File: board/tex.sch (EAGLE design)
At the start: 267 parts, among them K1 HLS8L-DC5V-S-C, K2 HLS8L-DC5V-S-C, K3 HLS8L-DC5V-S-C, K4 HLS8L-DC5V-S-C, Q47 FDD4141, U14 24LC32A, U15 OPTO-LTV817, U16 OPTO-LTV817, U17 OPTO-LTV817, U18 OPTO-LTV817, U19 RELAY-S108T02PTH, U20 RELAY-S108T02PTH, U21 IO-HC4051, U5 AZ23C5V1, Y1 32.768KHz

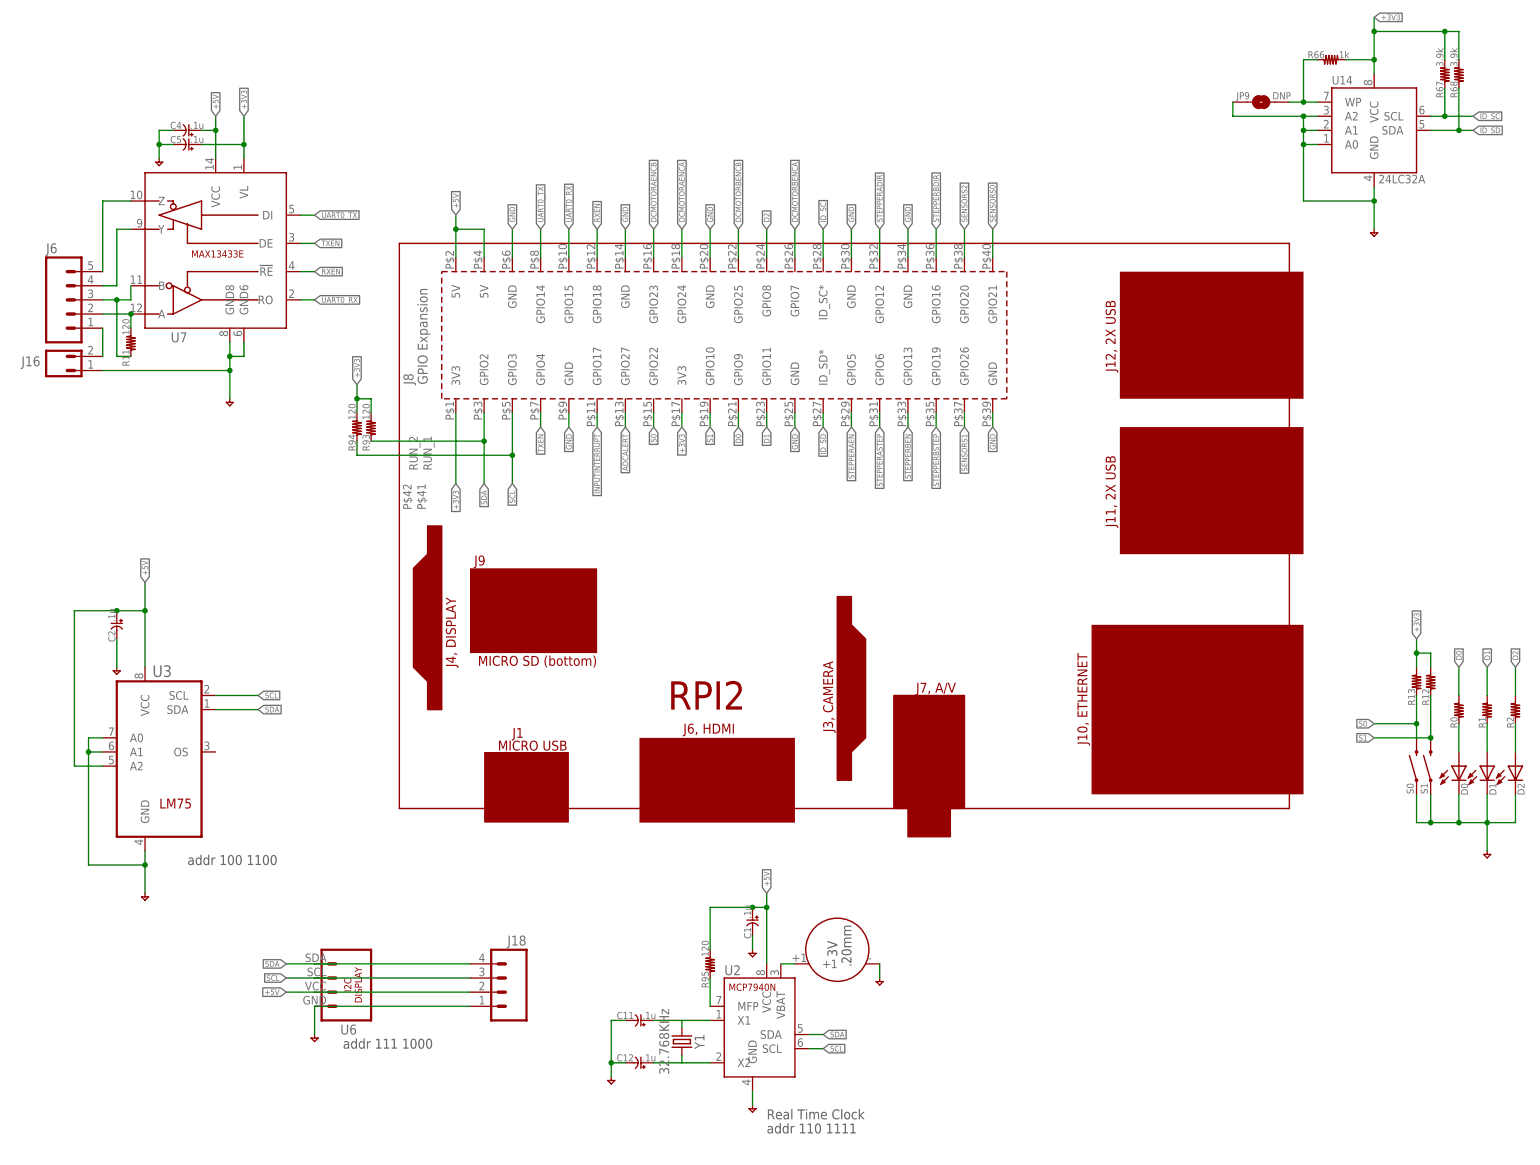
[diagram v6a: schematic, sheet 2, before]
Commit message: ready to place names
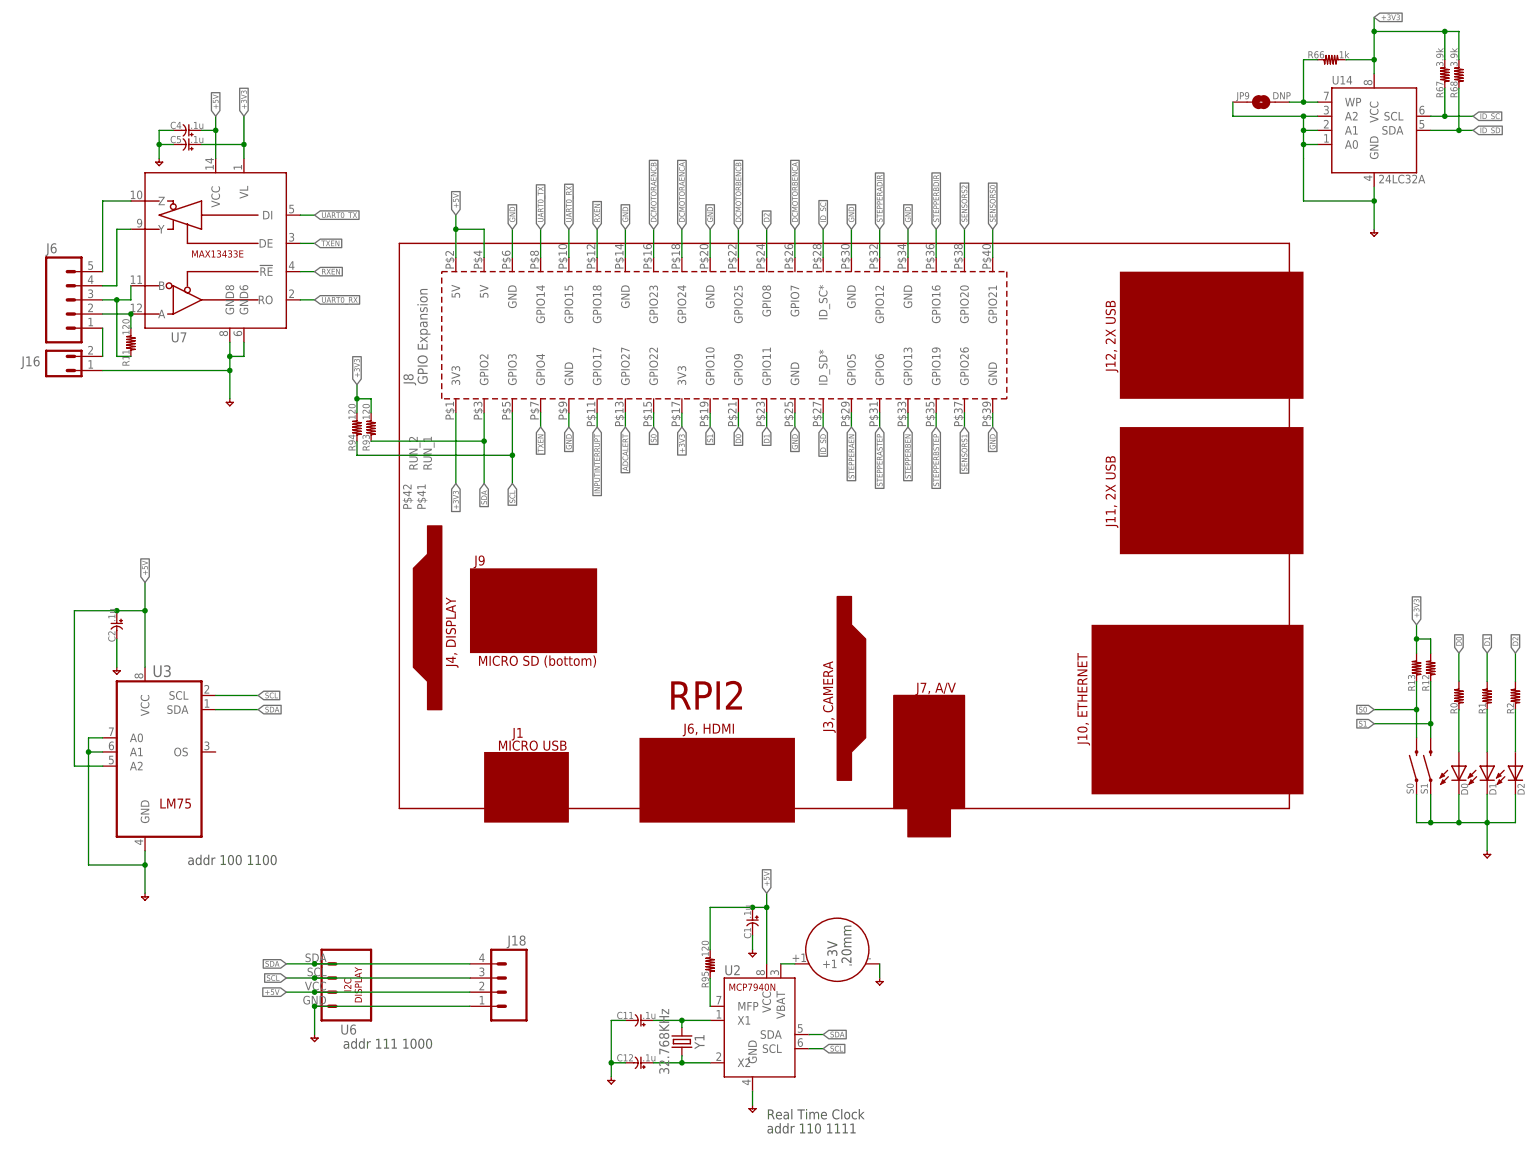
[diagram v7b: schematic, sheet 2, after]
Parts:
- added JP1, JP2: FIDUCIALUFIDUCIAL, holla:FIDUCIALUFIDUCIAL
- added TP1: (no value), holla:TESTPOINTTHRU
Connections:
- removed net ADC0_3: U8.AIN3
- net AGND: now also U8.AIN3
- net GND: now also TP1.P$1, U2.GND
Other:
- note added: "ENCODER"
- note added: "I2C Address Table 010 0000 I/O MCP23107 100 0000 VBATT Current Sense INA219 100 1000 ADC ADS1015 100 1100 TEMP LM75 110 0000 LED PCA9685 110 1111 RTC MCP7940 111 1000 Display SSD1306 Banggood"
- note added: "Relays can be VBATT voltage or +5V, install 0ohm resistor to select"
- note added: "ToDo List"
- note removed: "AGND not implemented, not high-performance design I2C Address Table 010 0000 I/O MCP23107 100 0000 VBATT Current Sense INA219 100 1000 ADC ADS1015 100 1100 TEMP LM75 110 0000 LED PCA9685 110 1111 RTC MCP7940 111 1000 Display SSD1306 Banggood"
- note removed: "SPI"
- note removed: "connect adc alert to rpi does ina219 give the vbatt voltage? do something adc0_3"
- note removed: "put down analog gnds add +5V out connector for stepper driver"
- moved on the sheet: C30, C34, C35, C36, C37, R0, R1, R12, R13, R2, R6, R7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

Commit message: board file submission
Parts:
- removed C35, C38: (no value), holla:C-USC0603
- removed D0, D37: (no value), holla:LED-0603
- removed J31: (no value), holla:M06-PLUGIN-SCREW
- removed J32: (no value), holla:M05-PLUGIN-SCREW
- removed JP9: DNP, holla:JUMPER-PAD-2-NO
- removed R0: (no value), holla:R-US_R0603
- removed R95: 120, holla:R-US_R0603
- removed S0: (no value), holla:SWITCH-PUSHBUTTON-6MMX3.5MM
- removed U21: IO-HC4051, holla:IO-HC4051
- removed U22: (no value), holla:IO-MCP23017SO
- added C13, C14: .1u, holla:C-USC0603
- added D3, D7: (no value), holla:LED-0603
- added J20: (no value), holla:M02-6.35MM
- added J22: (no value), holla:M02-PLUGIN-SCREW
- added JP3: FIDUCIALUFIDUCIAL, holla:FIDUCIALUFIDUCIAL
- added R14, R15: (no value), holla:R-US_R0603
- added S2: (no value), holla:SWITCH-PUSHBUTTON-6MMX3.5MM
- added U12: OPTO-LTV817, holla:OPTO-LTV817
- added U9: (no value), holla:DCDC-CONVERTER-LM2577-BOARD
- C10, C3: value (none) -> .1u
- C11, C15, C17, C2: value .1u -> (none)
- D21, D22, D23, D24: device holla:LED-0603 -> holla:DIODE-0603
- D28, D29, D30: device holla:DIODE-0603 -> holla:LED-0603
- D31: device holla:DIODE-0603 -> holla:DIODE-SMA
- D35, D36: device holla:LED-0603 -> holla:DIODE-0805
- D4: device holla:DIODE-SMA -> holla:LED-0603
- D5, D6: device holla:DIODE-0805 -> holla:LED-0603
- J1: device holla:M02-6.35MM -> holla:M04-PLUGIN-SCREW
- J10, J27, J28: device holla:M02-PLUGIN-SCREW -> holla:M03-PLUGIN-SCREW
- J11: device holla:M03-PLUGIN-SCREW -> holla:M04-0.1
- J12: device holla:M03-PLUGIN-SCREW -> holla:M02-0.1
- J13: device holla:M03-PLUGIN-SCREW -> holla:M05-PLUGIN-SCREW
- J14: device holla:M03-PLUGIN-SCREW -> holla:M04-PLUGIN-SCREW
- J15: device holla:M02-PLUGIN-SCREW -> holla:M04-PLUGIN-SCREW
- J16: device holla:M02-0.1 -> holla:M06-PLUGIN-SCREW
- J17: device holla:M06-PLUGIN-SCREW -> holla:M05-PLUGIN-SCREW
- J18: device holla:M04-0.1 -> holla:M05-PLUGIN-SCREW
- J21: device holla:M06-PLUGIN-SCREW -> holla:M02-PLUGIN-SCREW
- J29, J30: device holla:M03-PLUGIN-SCREW -> holla:M06-PLUGIN-SCREW
- J5: device holla:M04-PLUGIN-SCREW -> holla:M02-PLUGIN-SCREW
- J6: device holla:M05-PLUGIN-SCREW -> holla:M02-PLUGIN-SCREW
- J7: device holla:M05-PLUGIN-SCREW -> holla:M03-PLUGIN-SCREW
- J8, J9: device holla:M04-PLUGIN-SCREW -> holla:M03-PLUGIN-SCREW
- JP2: value FIDUCIALUFIDUCIAL -> DNP; device holla:FIDUCIALUFIDUCIAL -> holla:JUMPER-PAD-2-NO
- Q1, Q3: device holla:FET-NCHANNEL-SOT23 -> holla:FET-NCHANNEL-TO252
- Q12, Q14, Q16, Q18, Q20, Q33, Q36: device holla:FET-PCHANNEL-TO252 -> holla:FET-NCHANNEL-SOT23
- Q2, Q4: device holla:FET-PCHANNEL-TO252 -> holla:FET-NCHANNEL-TO252
- Q21, Q23, Q25, Q28, Q5, Q7, Q9: device holla:FET-NCHANNEL-SOT23 -> holla:FET-PCHANNEL-TO252
- Q26, Q29: device holla:FET-NCHANNEL-TO252 -> holla:FET-PCHANNEL-TO252
- Q32, Q35: device holla:FET-NCHANNEL-TO252 -> holla:FET-NCHANNEL-SOT23
- Q41: value (none) -> FDD4141; device holla:FET-NCHANNEL-SOT23 -> brightleaf:FDD4141TO252
- Q47: value FDD4141 -> (none); device brightleaf:FDD4141TO252 -> holla:FET-NCHANNEL-SOT23
- R10: value 47k -> (none)
- R11, R93, R94: value 120 -> (none)
- R19: value (none) -> 0
- R20, R21, R29, R31, R32, R66: value 1k -> (none)
- R22, R91: value 0 -> (none)
- R23, R90: value DNP -> (none)
- R24, R30: value 10k -> (none)
- R28: value 1k -> DNP
- R33: value 10k -> (none); device holla:R-US_R0603 -> holla:R-US_R1210
- R34, R51: device holla:R-US_R0603 -> holla:R-US_R1210
- R39, R40, R52: value (none) -> 120
- R43: value (none) -> 47k
- R44, R55, R56, R57, R71, R72, R77: value (none) -> 1k
- R53, R54, R69: value (none) -> 10k
- R59: device holla:R-US_R1210 -> holla:R-US_R0603
- R63: value (none) -> 0; device holla:R-US_R1210 -> holla:R-US_R0603
- R67, R68: value 3.9k -> (none)
- R70: value (none) -> DNP
- R73, R74: value (none) -> 3.9k
- R79: value (none) -> 120; device holla:R-US_R1210 -> holla:R-US_R0603
- U1: value (none) -> RELAY-S108T02PTH; device holla:DCDC-CONVERTER-LM2577-BOARD -> holla:RELAY-S108T02PTH
- U10: device holla:AMP-OPAMP-DUAL-SO08 -> holla:ADC-ADS1015-MSOP10
- U13: value (none) -> OPTO-LTV817; device holla:IO-PCA9685-TSSOP28 -> holla:OPTO-LTV817
- U14: value 24LC32A -> OPTO-LTV817; device holla:MEMORY-EEPROM-SO08 -> holla:OPTO-LTV817
- U16: value OPTO-LTV817 -> (none); device holla:OPTO-LTV817 -> holla:IO-MCP23017SO
- U17: value OPTO-LTV817 -> 24LC32A; device holla:OPTO-LTV817 -> holla:MEMORY-EEPROM-SO08
- U18: value OPTO-LTV817 -> IO-HC4051; device holla:OPTO-LTV817 -> holla:IO-HC4051
- U19: value RELAY-S108T02PTH -> (none); device holla:RELAY-S108T02PTH -> holla:RTC-MCP7940N
- U2: value (none) -> RELAY-S108T02PTH; device holla:RTC-MCP7940N -> holla:RELAY-S108T02PTH
- U20: value RELAY-S108T02PTH -> (none); device holla:RELAY-S108T02PTH -> holla:DISP-I2C-4PIN
- U3: device holla:SENSOR-TEMP-LM75-SO08 -> holla:COMM-MAX13433E
- U4: value (none) -> AZ23C5V1; device holla:ADC-INA219-SOIC8 -> brightleaf:AZ23CXXX
- U5: value AZ23C5V1 -> (none); device brightleaf:AZ23CXXX -> holla:IO-PCA9685-TSSOP28
- U6: device holla:DISP-I2C-4PIN -> holla:AMP-OPAMP-DUAL-SO08
- U7: device holla:COMM-MAX13433E -> holla:ADC-INA219-SOIC8
- U8: device holla:ADC-ADS1015-MSOP10 -> holla:SENSOR-TEMP-LM75-SO08
- renumbered B1 to B100, C30 to C19, C31 to C18, C34 to C23, C36 to C21, C37 to C20
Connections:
- net +3V3: now also C1.1, R39.2, R40.2, R41.2, R42.2, R73.2, R74.2, R77.2, U17.VCC, U3.VL; no longer C5.1, R12.2, R13.2, R66.2, R67.2, R68.2, R93.2, R94.2, U14.VCC, U7.VL
- net +5V: now also C16.1, C6.1, C8.1, J11.2, J16.4, J16.5, J16.6, J17.5, J18.5, J27.3, J28.3, J30.6, R28.2, R78.1, R79.2, U1.+, U16.!RESET, U16.VDD, U19.VCC, U2.+, U20.VCC, U5.A5, U5.VCC, U7.VS, U8.A2, U8.VCC, U9.VOUT+; no longer C1.1, C22.1, C4.1, J18.2, J19.4, J19.5, J19.6, J29.3, J30.3, J31.6, J32.5, J7.5, R3.1, R90.2, R95.2, U1.VOUT+, U13.A5, U13.VCC, U19.+, U2.VCC, U20.+, U22.!RESET, U22.VDD, U3.A2, U4.VS, U6.VCC, U7.VCC
- net ADC0_1: now also R53.2, U10.AIN1, U6A.OUT; no longer R30.2, U10A.OUT, U8.AIN1
- net ADC0_2: now also R54.2, U10.AIN2, U6B.OUT; no longer R33.2, U10B.OUT, U8.AIN2
- net ADCALERT: now also U10.ALERT; no longer U8.ALERT
- net AGND: now also C11.2, C12.2, C22.2, C4.2, C5.2, J21.1, J22.1, R55.1, R56.1, R59.1, R64.2, R70.1, R71.1, R75.1, R87.1, R89.1, U10.ADDR, U10.AIN3, U10.GND, U18.!E, U18.GND, U18.VEE, U6A.V-; no longer C16.2, C35.2, C38.2, C6.2, C8.2, J29.1, J30.1, R17.1, R19.1, R21.1, R23.1, R25.2, R27.1, R28.1, R31.1, R5.1, U10A.V-, U21.!E, U21.GND, U21.VEE, U8.ADDR, U8.AIN3, U8.GND
- net AVCC: now also C15.1, C5.1, C7.1, R78.2, R90.2, R91.2, R93.2, R94.2, U10.VCC, U18.VCC, U6A.V+; no longer C16.1, C38.1, C8.1, R3.2, R6.2, R7.2, R8.2, R9.2, U10A.V+, U21.VCC, U8.VCC
- net D0: now also R60.2; no longer R0.2
- net D1: now also R61.2; no longer R1.2
- net D2: now also R62.2; no longer R2.2
- net DCMOTORAENCA: now also U14.4; no longer U15.4
- net DCMOTORAENCB: now also U15.4; no longer U16.4
- net DCMOTORBENCA: now also U12.4; no longer U17.4
- net DCMOTORBENCB: now also U13.4; no longer U18.4
- net GND: now also C13.2, C14.2, C16.2, C6.2, C8.2, D31.A, D32.C, D33.C, D34.C, J11.1, J12.1, J14.4, J15.4, J17.1, J19.1, J19.2, J19.3, J19.4, J19.5, J19.6, J20.1, J30.1, JP2.1, Q12.S, Q14.S, Q16.S, Q18.S, Q20.S, Q32.S, Q33.S, Q35.S, Q36.S, Q47.S, R1.1, R10.1, R11.1, R12.1, R13.1, R14.1, R16.1, R17.1, R2.1, R3.1, R33.2, R34.2, R4.1, R43.2, R5.1, R6.1, R64.1, R7.1, R8.1, R80.1, R81.1, R82.1, R83.1, R84.1, R85.1, R9.1, S2.1, U12.2, U12.3, U13.2, U13.3, U14.2, U14.3, U16.A0, U16.A1, U16.A2, U16.VSS, U17.A0, U17.A1, U17.A2, U17.GND, U19.GND, U20.GND, U3.GND6, U3.GND8, U5.!OE, U5.A0, U5.A1, U5.A2, U5.A3, U5.A4, U5.EXTCLK, U5.GND, U7.A0, U7.A1, U7.GND, U8.A0, U8.A1, U8.GND, U9.VIN-, U9.VOUT-; no longer C11.2, C12.2, C22.2, C4.2, C5.2, D0.C, D1.C, D2.C, D4.A, J1.1, J16.1, J21.1, J21.2, J21.3, J21.4, J21.5, J21.6, J31.1, J32.1, J7.1, J8.4, J9.4, JP9.1, Q1.S, Q21.S, Q23.S, Q25.S, Q28.S, Q3.S, Q41.S, Q5.S, Q7.S, Q9.S, R10.2, R25.1, R35.1, R37.1, R39.1, R41.1, R43.1, R45.1, R47.1, R49.1, R51.1, R53.1, R55.1, R57.1, R59.2, R63.2, R69.1, R70.1, R71.1, R72.1, R73.1, R74.1, R75.1, R76.1, R77.1, R78.1, S0.1, U1.VIN-, U1.VOUT-, U13.!OE, U13.A0, U13.A1, U13.A2, U13.A3, U13.A4, U13.EXTCLK, U13.GND, U14.A0, U14.A1, U14.A2, U14.GND, U16.2, U16.3, U17.2, U17.3, U18.2, U18.3, U2.GND, U22.A0, U22.A1, U22.A2, U22.VSS, U3.A0, U3.A1, U3.GND, U4.A0, U4.A1, U4.GND, U6.GND, U7.GND6, U7.GND8
- net GND4: now also D21.A, D27.C, K2.V-, Q18.D; no longer D31.A, D35.C, K4.V-, Q46.D
- net ID_SC: now also R73.1, U17.SCL; no longer R67.1, U14.SCL
- net ID_SD: now also R74.1, U17.SDA; no longer R68.1, U14.SDA
- net INPUTINTERRUPT: now also U16.INTB; no longer U22.INTB
- net MOTORA_SENSE: now also Q1.S, Q2.S, R33.1, R44.1; no longer Q32.S, Q35.S, R29.1, R63.1
- net MOTORB_SENSE: now also Q3.S, Q4.S, R34.1, R57.1; no longer Q26.S, Q29.S, R32.1, R59.1
- net N$1: now also Q40.G, U5.PWM0; no longer Q1.G, U13.PWM0
- net N$100: now also D6.C, R3.2; no longer D18.C, R55.2
- net N$101: now also J20.2; no longer J1.2
- net N$102: now also C29.1, J29.1, U16.GPB2; no longer C24.1, J17.1, U22.GPB2
- net N$103: now also C28.1, J29.2, U16.GPB3; no longer C25.1, J17.2, U22.GPB3
- net N$104: now also JP2.2, R77.1, U17.WP; no longer JP9.2, R66.1, U14.WP
- net N$105: now also R53.1, R56.2, U6A.-IN; no longer R28.2, R30.1, U10A.-IN
- net N$107: now also C9.1, R57.2, U6B.+IN; no longer C17.1, R32.2, U10B.+IN
- net N$108: now also C27.1, J29.3, U16.GPB4; no longer C26.1, J17.3, U22.GPB4
- net N$109: now also C26.1, J29.4, U16.GPB5; no longer C27.1, J17.4, U22.GPB5
- net N$111: now also C25.1, J29.5, U16.GPB6; no longer C28.1, J17.5, U22.GPB6
- net N$114: now also C24.1, J29.6, U16.GPB7; no longer C29.1, J17.6, U22.GPB7
- net N$118: now also U19.VBAT; no longer U2.VBAT
- net N$120: now also J28.2, R90.1, U18.Y0; no longer J30.2, R92.1, U21.Y0
- net N$124: now also R88.1, R89.2, U18.Y1; no longer R18.1, R19.2, U21.Y1
- net N$13: now also J13.2, R52.2, U3.A; no longer J6.2, R11.2, U7.A
- net N$130: now also C17.1, R86.1, R87.2, U18.Y2; no longer C6.1, R4.1, R5.2, U21.Y2
- net N$138: now also C11.1, R75.2, R76.1; no longer C7.1, R16.1, R17.2
- net N$139: now also D7.C, R4.2; no longer D17.C, R53.2
- net N$14: now also J13.3, R52.1, U3.B; no longer J6.3, R11.1, U7.B
- net N$140: now also D8.C, R5.2; no longer D16.C, R51.2
- net N$141: now also D9.C, R6.2; no longer D15.C, R49.2
- net N$142: now also D10.C, R7.2; no longer D14.C, R47.2
- net N$143: now also J10.2, K4.COM; no longer J14.2, K1.COM
- net N$144: now also J10.1, K4.NO; no longer J14.1, K1.NO
- net N$145: now also J10.3, K4.NC; no longer J14.3, K1.NC
- net N$146: now also D11.C, R8.2; no longer D13.C, R45.2
- net N$147: now also D29.A, R31.1; no longer D33.A, R85.1
- net N$148: now also R67.1, U14.1; no longer R80.1, U15.1
- net N$149: now also J15.3, R68.2; no longer J8.3, R81.2
- net N$15: now also J13.4, U3.Y; no longer J6.4, U7.Y
- net N$150: now also J15.2, R67.2; no longer J8.2, R80.2
- net N$151: now also J17.2, Q42.D; no longer J32.2, Q39.D
- net N$152: now also J18.4, Q47.D; no longer J7.4, Q40.D
- net N$153: now also J18.3, Q46.D; no longer J7.3, Q41.D
- net N$154: now also J18.2, Q45.D; no longer J7.2, Q42.D
- net N$155: now also R68.1, U15.1; no longer R81.1, U16.1
- net N$156: now also J14.2, R65.2; no longer J9.2, R82.2
- net N$157: now also J14.3, R66.2; no longer J9.3, R83.2
- net N$158: now also R65.1, U12.1; no longer R82.1, U17.1
- net N$159: now also D22.A, D28.C, K1.V-, Q19.D; no longer D30.A, D34.C, K3.V-, Q45.D
- net N$16: now also J13.5, U3.Z; no longer J6.5, U7.Z
- net N$161: now also D23.A, D29.C, K3.V-, Q17.D; no longer D29.A, D33.C, K2.V-, Q44.D
- net N$162: now also R66.1, U13.1; no longer R83.1, U18.1
- net N$163: now also J9.2, K3.COM; no longer J11.2, K2.COM
- net N$164: now also J9.1, K3.NO; no longer J11.1, K2.NO
- net N$165: now also J9.3, K3.NC; no longer J11.3, K2.NC
- net N$166: now also J8.2, K1.COM; no longer J12.2, K3.COM
- net N$167: now also J8.1, K1.NO; no longer J12.1, K3.NO
- net N$168: now also J8.3, K1.NC; no longer J12.3, K3.NC
- net N$169: now also J7.1, K2.NO; no longer J13.1, K4.NO
- net N$17: now also J12.2, J13.1; no longer J16.2, J6.1
- net N$170: now also J7.2, K2.COM; no longer J13.2, K4.COM
- net N$171: now also J7.3, K2.NC; no longer J13.3, K4.NC
- net N$172: now also D21.C, D22.C, D23.C, D24.C, R19.1, R28.1, R29.2, R30.2, R31.2, R32.2; no longer D28.C, D29.C, D30.C, D31.C, R84.2, R85.2, R86.2, R87.2, R90.1, R91.1
- net N$173: now also D30.A, R32.1; no longer D32.A, R84.1
- net N$174: now also D28.A, R30.1; no longer D34.A, R86.1
- net N$175: now also D27.A, R29.1; no longer D35.A, R87.1
- net N$176: now also D24.A, D30.C, K4.V-, Q20.D; no longer D28.A, D32.C, K1.V-, Q43.D
- net N$177: now also J6.2, U2.T2; no longer J10.2, U19.T2
- net N$178: now also J5.1, U1.T1; no longer J15.1, U20.T1
- net N$179: now also J5.2, U1.T2; no longer J15.2, U20.T2
- net N$180: now also D26.C, R26.2; no longer D36.C, R88.2
- net N$181: now also D25.C, R25.2; no longer D37.C, R89.2
- net N$182: now also D26.A, U2.-; no longer D36.A, U19.-
- net N$183: now also D25.A, U1.-; no longer D37.A, U20.-
- net N$184: now also J24.2, R94.1, U18.Y4; no longer J26.2, R6.1, U21.Y4
- net N$185: now also C22.1, J23.2, R93.1, U18.Y5; no longer C35.1, J25.2, R7.1, U21.Y5
- net N$186: now also J22.2, R92.1, U18.Y6; no longer J24.2, R8.1, U21.Y6
- net N$187: now also J21.2, R91.1, U18.Y7; no longer J23.2, R9.1, U21.Y7
- net N$188: now also R58.2, R63.2; no longer R22.2, R26.2
- net N$189: now also R72.1, U18.Z; no longer R20.1, U21.Z
- net N$190: now also R58.1, R59.2, U10.AIN0; no longer R26.1, R27.2, U8.AIN0
- net N$191: now also R69.2, U18.Y3; no longer R24.2, U21.Y3
- net N$192: now also R79.1, U19.MFP; no longer R95.1, U2.MFP
- net N$194: now also Q41.D; no longer Q47.D
- net N$2: now also D35.C, R86.2; no longer D5.C, R4.2
- net N$20: now also D35.A, J26.2; no longer D5.A, J28.2
- net N$25: now also D36.C, R76.2; no longer D6.C, R16.2
- net N$26: now also D36.A, J25.2; no longer D6.A, J27.2
- net N$27: now also J27.2, R88.2; no longer J29.2, R18.2
- net N$29: now also D32.A, R60.1; no longer D0.A, R0.1
- net N$3: now also C13.1, U19.X1; no longer C11.1, U2.X1
- net N$30: now also D33.A, R61.1; no longer D1.A, R1.1
- net N$31: now also D34.A, R62.1; no longer D2.A, R2.1
- net N$35: now also Q12.D, Q6.G, R20.1; no longer Q19.D, Q20.G, R52.1
- net N$36: now also Q26.G, Q36.D, R45.1; no longer Q17.D, Q18.G, R50.1
- net N$37: now also Q13.D, Q7.G, R21.1; no longer Q15.D, Q16.G, R48.1
- net N$38: now also R63.1, R70.2; no longer R22.1, R23.2
- net N$39: now also R69.1, R71.2; no longer R21.2, R24.1
- net N$4: now also Q41.G, R43.1, U4.A; no longer Q47.G, R10.1, U5.A
- net N$40: now also Q27.G, Q37.D, R47.1; no longer Q13.D, Q14.G, R46.1
- net N$41: now also Q14.D, Q8.G, R22.1; no longer Q11.D, Q12.G, R44.1
- net N$42: now also Q28.G, Q38.D, R48.1; no longer Q10.G, Q9.D, R42.1
- net N$43: now also Q15.D, Q9.G, R23.1; no longer Q7.D, Q8.G, R40.1
- net N$44: now also Q29.G, Q39.D, R49.1; no longer Q5.D, Q6.G, R38.1
- net N$45: now also Q10.G, Q16.D, R24.1; no longer Q3.D, Q4.G, R36.1
- net N$46: now also Q30.G, Q40.D, R50.1; no longer Q1.D, Q2.G, R34.1
- net N$47: now also Q16.G, U5.PWM1; no longer Q3.G, U13.PWM1
- net N$48: now also Q39.G, U5.PWM2; no longer Q5.G, U13.PWM2
- net N$49: now also Q15.G, U5.PWM3; no longer Q7.G, U13.PWM3
- net N$5: now also C14.1, U19.X2; no longer C12.1, U2.X2
- net N$50: now also Q38.G, U5.PWM4; no longer Q9.G, U13.PWM4
- net N$51: now also Q14.G, U5.PWM5; no longer Q11.G, U13.PWM5
- net N$52: now also Q37.G, U5.PWM6; no longer Q13.G, U13.PWM6
- net N$53: now also Q13.G, U5.PWM7; no longer Q15.G, U13.PWM7
- net N$54: now also Q36.G, U5.PWM8; no longer Q17.G, U13.PWM8
- net N$55: now also C12.1, R72.2; no longer C9.1, R20.2
- net N$56: now also Q12.G, U5.PWM9; no longer Q19.G, U13.PWM9
- net N$57: now also D2.A, J1.2, Q2.D, Q22.D, R15.2; no longer D26.A, J5.2, Q32.D, Q33.D, R64.2
- net N$58: now also Q2.G, Q22.G, Q33.D, R37.1; no longer Q31.D, Q32.G, Q33.G, R62.1
- net N$59: now also D1.A, D17.C, D19.A, J1.1, Q1.D, Q21.D; no longer D22.C, D23.A, D27.A, J5.1, Q35.D, Q36.D
- net N$6: now also J30.2, U16.GPA6; no longer J31.2, U22.GPA6
- net N$60: now also Q1.G, Q21.G, Q32.D, R36.1; no longer Q34.D, Q35.G, Q36.G, R65.1
- net N$61: now also Q32.G, U5.PWM15; no longer Q34.G, U13.PWM15
- net N$62: now also Q33.G, U5.PWM14; no longer Q31.G, U13.PWM14
- net N$63: now also D4.A, J1.4, Q24.D, Q4.D, R18.2; no longer D25.A, J5.4, Q26.D, Q27.D, R60.2
- net N$64: now also Q24.G, Q31.D, Q4.G, R35.1; no longer Q25.D, Q26.G, Q27.G, R58.1
- net N$65: now also D16.A, J4.4, Q30.D; no longer D8.A, J2.4, Q2.D
- net N$66: now also D15.A, J4.3, Q10.D; no longer D9.A, J2.3, Q4.D
- net N$67: now also D14.A, J4.2, Q29.D; no longer D10.A, J2.2, Q6.D
- net N$68: now also D13.A, J4.1, Q9.D; no longer D11.A, J2.1, Q8.D
- net N$69: now also Q28.D; no longer Q10.D
- net N$7: now also J30.5, U16.GPB1; no longer J31.5, U22.GPB1
- net N$70: now also D11.A, Q8.D; no longer D13.A, Q12.D
- net N$71: now also D10.A, Q27.D; no longer D14.A, Q14.D
- net N$72: now also D9.A, Q7.D; no longer D15.A, Q16.D
- net N$73: now also D8.A, J2.4, Q26.D; no longer D16.A, J4.4, Q18.D
- net N$74: now also D7.A, J2.3, Q6.D; no longer D17.A, J4.3, Q20.D
- net N$75: now also D13.C, R10.2; no longer D11.C, R41.2
- net N$76: now also J6.1, U2.T1; no longer J10.1, U19.T1
- net N$77: now also R9.2; no longer R43.2
- net N$78: now also D1.C, R14.2; no longer D27.C, R72.2
- net N$79: now also D2.C, R16.2; no longer D26.C, R71.2
- net N$8: now also J30.4, U16.GPB0; no longer J31.4, U22.GPB0
- net N$80: now also D3.C, R17.2; no longer D24.C, R69.2
- net N$81: now also D4.C, R1.2; no longer D25.C, R70.2
- net N$82: now also D14.C, R11.2; no longer D10.C, R39.2
- net N$83: now also D15.C, R12.2; no longer D9.C, R37.2
- net N$84: now also D16.C, R13.2; no longer D8.C, R35.2
- net N$85: now also D18.C, D20.A, D3.A, J1.3, Q23.D, Q3.D; no longer D20.C, D21.A, D24.A, J5.3, Q29.D, Q30.D
- net N$86: now also Q23.G, Q3.G, Q34.D, R38.1; no longer Q28.D, Q29.G, Q30.G, R61.1
- net N$87: now also Q34.G, U5.PWM13; no longer Q28.G, U13.PWM13
- net N$88: now also Q31.G, U5.PWM12; no longer Q25.G, U13.PWM12
- net N$89: now also D18.A, D20.C, R18.1; no longer D20.A, D21.C, R60.1
- net N$9: now also J30.3, U16.GPA7; no longer J31.3, U22.GPA7
- net N$90: now also Q35.G, U5.PWM10; no longer Q21.G, U13.PWM10
- net N$91: now also Q11.G, U5.PWM11; no longer Q23.G, U13.PWM11
- net N$92: now also D17.A, D19.C, R15.1; no longer D22.A, D23.C, R64.1
- net N$93: now also D6.A, J2.2, Q25.D; no longer D18.A, J4.2, Q22.D
- net N$94: now also D5.A, J2.1, Q5.D; no longer D19.A, J4.1, Q24.D
- net N$95: now also Q11.D, Q5.G, R27.1; no longer Q23.D, Q24.G, R56.1
- net N$96: now also Q25.G, Q35.D, R46.1; no longer Q21.D, Q22.G, R54.1
- net N$97: now also C4.1, R44.2, U6A.+IN; no longer C15.1, R29.2, U10A.+IN
- net N$98: now also D5.C, R2.2; no longer D19.C, R57.2
- net N$99: now also R54.1, R55.2, U6B.-IN; no longer R31.2, R33.1, U10B.-IN
- net RELAY0EN: now also Q20.G, U16.GPA0; no longer Q43.G, U22.GPA0
- net RELAY1EN: now also Q17.G, U16.GPA1; no longer Q44.G, U22.GPA1
- net RELAY2EN: now also Q19.G, U16.GPA2; no longer Q45.G, U22.GPA2
- net RELAY3EN: now also Q18.G, U16.GPA3; no longer Q46.G, U22.GPA3
- net RELAY4EN: now also R26.1, U16.GPA4; no longer R88.1, U22.GPA4
- net RELAY5EN: now also R25.1, U16.GPA5; no longer R89.1, U22.GPA5
- net RXEN: now also U3.!RE; no longer U7.!RE
- net S0: now also R41.1, S1.2; no longer R13.1, S0.2
- net S1: now also R42.1, S2.2; no longer R12.1, S1.2
- net SCL: now also J11.3, R40.1, U10.SCL, U16.SCL, U19.SCL, U20.SCL, U5.SCL, U7.SCL; no longer J18.3, R94.1, U13.SCL, U2.SCL, U22.SCL, U3.SCL, U4.SCL, U6.SCL
- net SDA: now also J11.4, R39.1, U10.SDA, U16.SDA, U19.SDA, U20.SDA, U5.SDA, U7.SDA; no longer J18.4, R93.1, U13.SDA, U2.SDA, U22.SDA, U3.SDA, U4.SDA, U6.SDA
- net SENSORS0: now also U18.S0; no longer U21.S0
- net SENSORS1: now also U18.S1; no longer U21.S1
- net SENSORS2: now also U18.S2; no longer U21.S2
- net STEPPER1DIROUT: now also J17.3, Q43.D; no longer J32.3, Q38.D
- net STEPPER1ENOUT: now also J17.4, Q44.D; no longer J32.4, Q37.D
- net STEPPERADIR: now also Q46.G, R84.2; no longer Q41.G, R77.2
- net STEPPERAEN: now also Q47.G, R85.2; no longer Q40.G, R76.2
- net STEPPERASTEP: now also Q45.G, R83.2; no longer Q42.G, R78.2
- net STEPPERBDIR: now also Q43.G, R81.2; no longer Q38.G, R74.2
- net STEPPERBEN: now also Q44.G, R82.2; no longer Q37.G, R73.2
- net STEPPERBSTEP: now also Q42.G, R80.2; no longer Q39.G, R75.2
- net TXEN: now also U3.DE; no longer U7.DE
- net UART0_RX: now also U3.RO; no longer U7.RO
- net UART0_TX: now also U3.DI; no longer U7.DI
- net VBATT: now also D31.C, J14.1, J15.1, J16.1, J16.2, J16.3, Q21.S, Q23.S, Q25.S, Q26.S, Q28.S, Q29.S, Q5.S, Q7.S, Q9.S, R19.2, R20.2, R21.2, R22.2, R23.2, R24.2, R27.2, R35.2, R37.2, R45.2, R47.2, R49.2, R51.2, U7.IN-, U9.VIN+; no longer D4.C, J19.1, J19.2, J19.3, J8.1, J9.1, Q12.S, Q14.S, Q16.S, Q18.S, Q2.S, Q20.S, Q33.S, Q36.S, Q4.S, R34.2, R40.2, R42.2, R44.2, R52.2, R54.2, R56.2, R58.2, R61.2, R62.2, R65.2, R79.2, R91.2, U1.VIN+, U4.IN-
- net VBATTISENSE: now also Q41.S, R51.1, U4.C1, U4.C2, U7.IN+; no longer Q47.S, R79.1, U4.IN+, U5.C1, U5.C2
